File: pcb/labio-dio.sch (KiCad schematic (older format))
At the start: 103 parts, among them P601 CONN_01X02, P602 CONN_01X02, P603 CONN_01X04, P604 CONN_01X02, P605 CONN_01X03, P606 CONN_01X03, P607 CONN_01X05, P608 CONN_01X05, Q601 Q_NMOS_GSD, Q602 Q_NMOS_GSD, Q603 Q_NMOS_GSD, Q604 Q_NMOS_GSD, Q605 Q_NMOS_GSD, Q606 Q_NMOS_GSD, Q607 Q_NMOS_GSD, Q608 Q_NMOS_GSD, Q609 Q_NMOS_GSD, Q610 Q_NMOS_GSD, Q611 Q_NMOS_GSD, Q612 Q_NMOS_GSD, Q613 Q_NMOS_GSD, SW601 DIP_SWITCH_X04, SW602 DIP_SWITCH_X04, SW603 DIP_SWITCH_X04, SW604 DIP_SWITCH_X04, SW605 ROT_ENC, SW606 DIP_SWITCH_X04, U601 L298P_PowerSO20

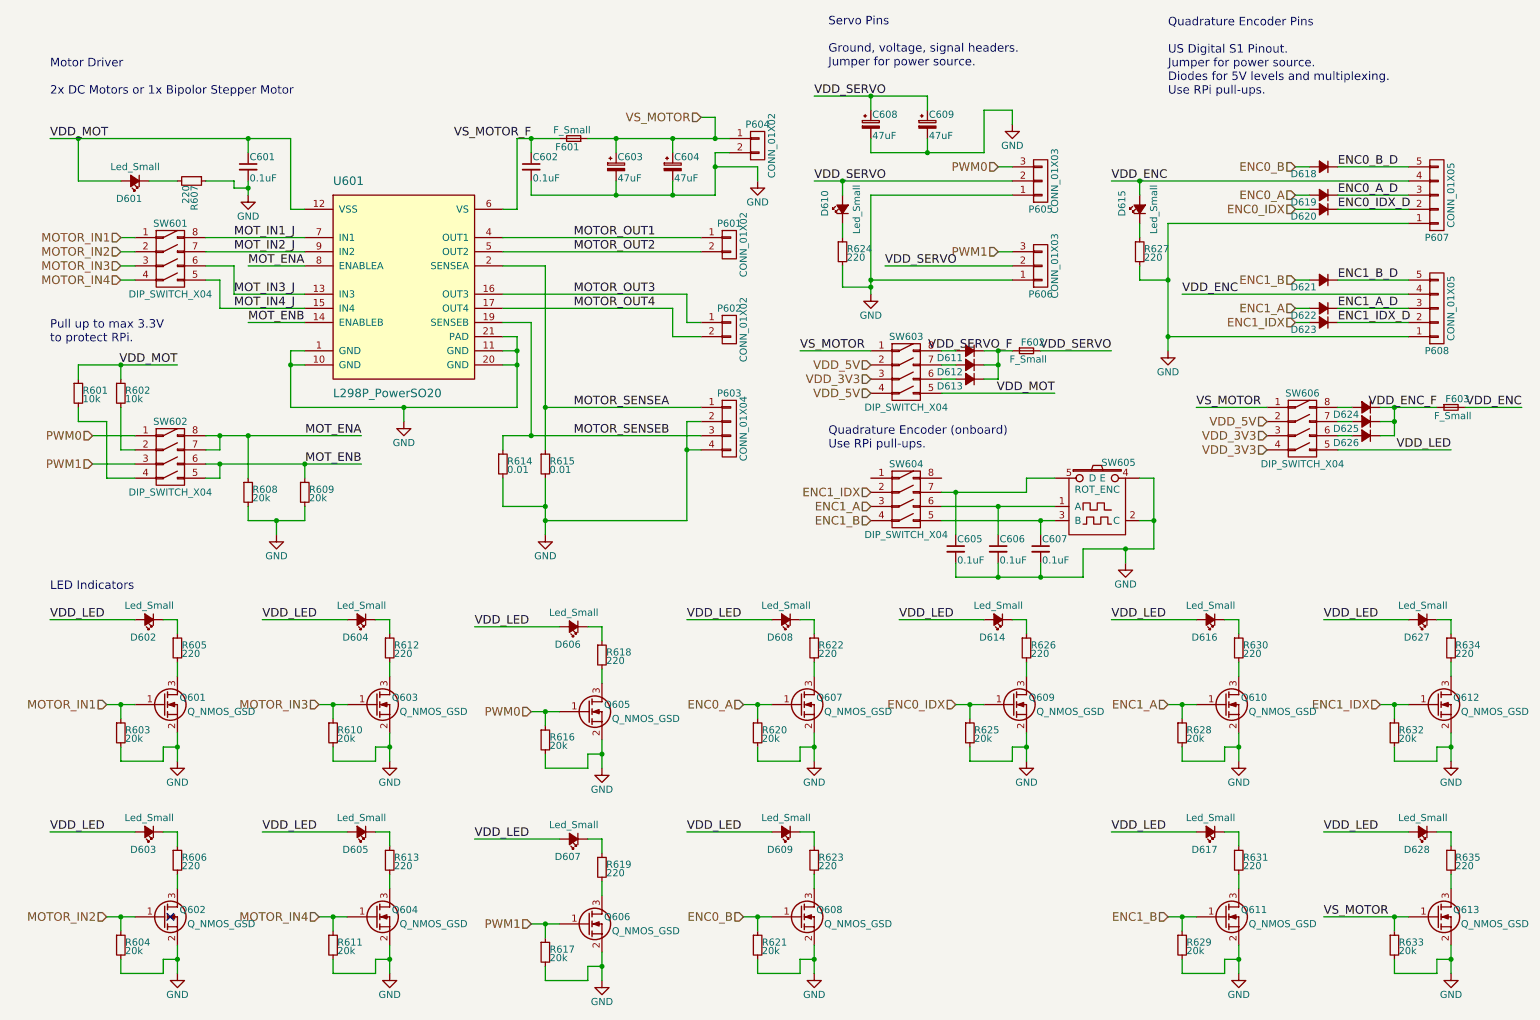
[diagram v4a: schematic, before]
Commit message: Fix ADC reading mic, possible backpowering, encoder pull downs, vias in footprint:
* Mic needs on-board path to ADC. Add proper bias and amp. Connect to ADC or codec with switches.
* Mic footprint (U701) flipped. Redraw footprint and adjust routing.
* Remove power from dip switches and replace with fuses. Turning power off to a block could result in backpower from driven IO lines.
* Remove/adjust pull downs on LEDs for encoder/dpad lines.
* Move vias out of display connector (P401) footprint.
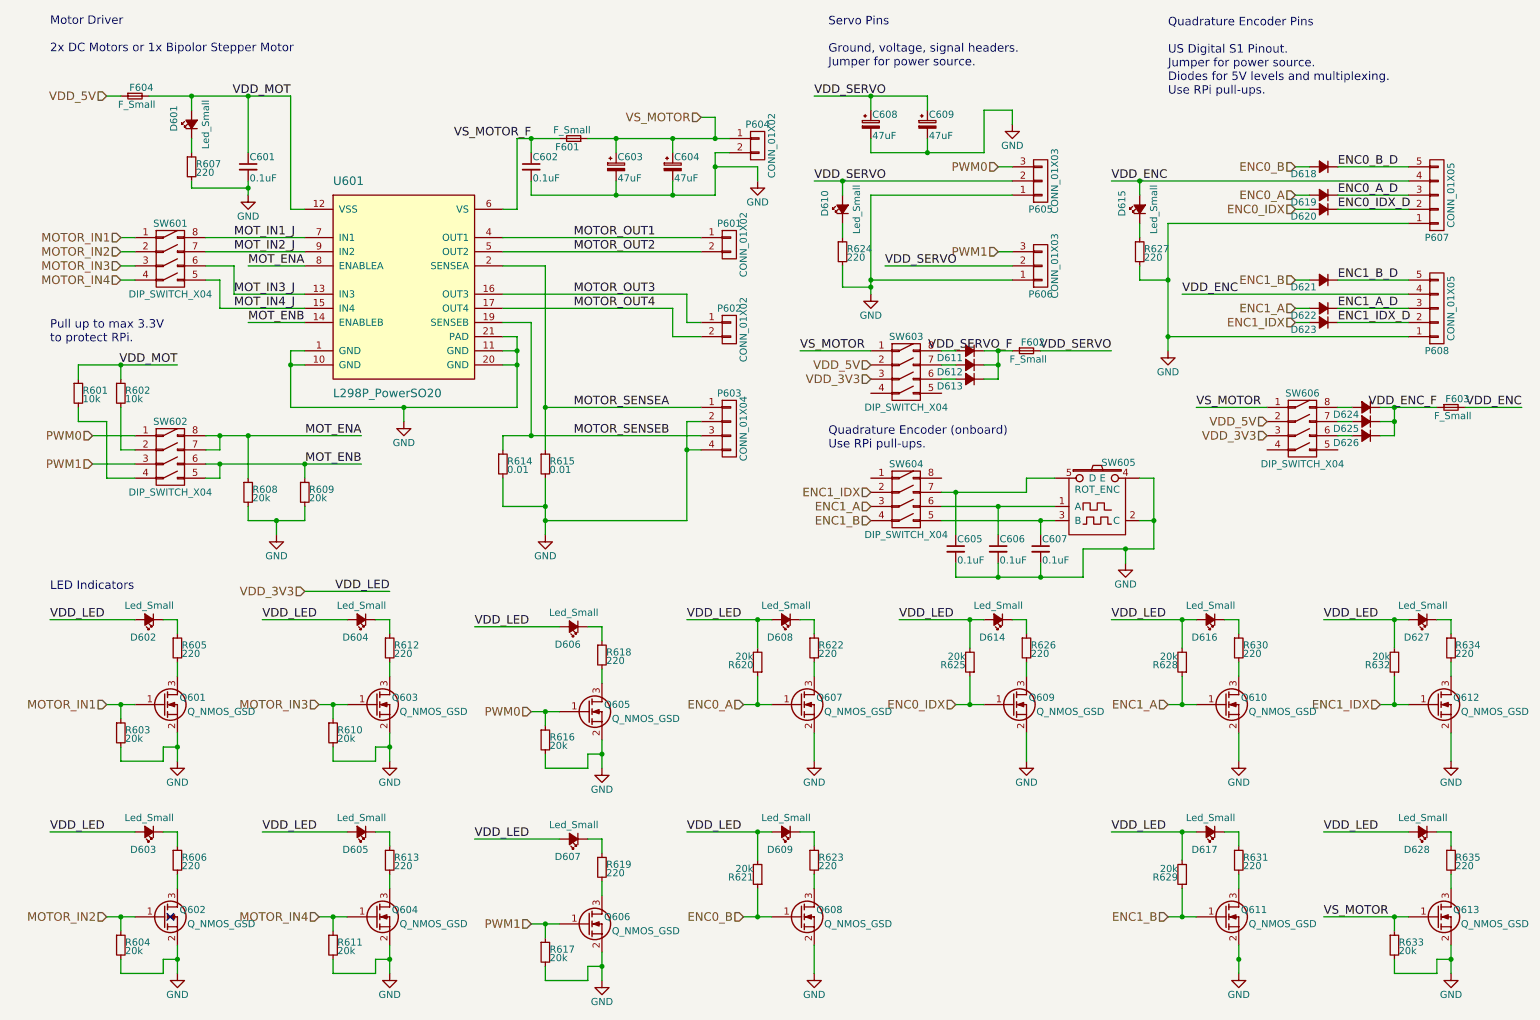
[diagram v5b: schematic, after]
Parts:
- added F604: F_Small, Resistors_SMD:R_1206, symbol F_Small
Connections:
- net GND: now also R607.2; no longer R607.1, R620.2, R621.2, R625.2, R628.2, R629.2, R632.2
- net VDD_3V3: now also D602.2 (A), D603.2 (A), D604.2 (A), D605.2 (A), D606.2 (A), D607.2 (A), D608.2 (A), D609.2 (A), D614.2 (A), D616.2 (A), D617.2 (A), D627.2 (A), D628.2 (A), R620.2, R621.2, R625.2, R628.2, R629.2, R632.2; no longer SW606.4 (4A)
- net VDD_5V: now also F604.1; no longer SW603.4 (4A)
- net VDD_MOT: now also F604.2; no longer SW603.5 (4B)
- net at D601.1 (K): now also R607.1; no longer R607.2
- removed net VDD_LED: D602.2 (A), D603.2 (A), D604.2 (A), D605.2 (A), D606.2 (A), D607.2 (A), D608.2 (A), D609.2 (A), D614.2 (A), D616.2 (A), D617.2 (A), D627.2 (A), D628.2 (A), SW606.5 (4B)
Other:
- moved on the sheet: D601, R607, R620, R621, R625, R628, R629, R632
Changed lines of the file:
@@
 encoding utf-8
 Sheet 6 10
-Title ""
+Title "Raspberry Pi Embedded Lab I/O"
 Date ""
-Rev ""
-Comp ""
+Rev "1.1.4"
+Comp "Carnegie Mellon University"
 Comment1 ""
-Comment2 ""
+Comment2 "Drawn by: Ian Hartwig"
 Comment3 ""
 Comment4 ""
@@
 Text Notes 6200 1000 0    60   ~ 0
 Servo Pins\n\nGround, voltage, signal headers.\nJumper for power source.
-Text Notes 700  1200 0    60   ~ 0
+Text Notes 700  900  0    60   ~ 0
 Motor Driver\n\n2x DC Motors or 1x Bipolor Stepper Motor
 $Comp
@@
 	1    0    0    -1
 $EndComp
-Text Label 7800 3300 2    60   ~ 0
-VDD_MOT
 Text Label 1600 3100 2    60   ~ 0
 VDD_MOT
-Text Label 700  1500 0    60   ~ 0
+Text Label 2400 1200 2    60   ~ 0
 VDD_MOT
-Text HLabel 9300 3700 0    60   Input ~ 0
+Text HLabel 2500 4700 0    60   Input ~ 0
 VDD_3V3
-Text Label 10600 3700 2    60   ~ 0
+Text Label 3100 4700 2    60   ~ 0
 VDD_LED
 Text Label 700  6400 0    60   ~ 0
@@
 L R_Small R620
 U 1 1 576F8F6D
-P 5700 5700
-F 0 "R620" H 5730 5720 50  0000 L CNN
-F 1 "20k" H 5730 5660 50  0000 L CNN
-F 2 "Resistors_SMD:R_0603" H 5700 5700 50  0001 C CNN
-F 3 "" H 5700 5700 50  0000 C CNN
-	1    5700 5700
-	1    0    0    -1
+P 5700 5200
+F 0 "R620" H 5730 5220 50  0000 L CNN
+F 1 "20k" H 5730 5160 50  0000 L CNN
+F 2 "Resistors_SMD:R_0603" H 5700 5200 50  0001 C CNN
+F 3 "" H 5700 5200 50  0000 C CNN
+	1    5700 5200
+	-1   0    0    1
 $EndComp
 $Comp
@@
 L R_Small R621
 U 1 1 576F8F95
-P 5700 7200
-F 0 "R621" H 5730 7220 50  0000 L CNN
-F 1 "20k" H 5730 7160 50  0000 L CNN
-F 2 "Resistors_SMD:R_0603" H 5700 7200 50  0001 C CNN
-F 3 "" H 5700 7200 50  0000 C CNN
-	1    5700 7200
-	1    0    0    -1
+P 5700 6700
+F 0 "R621" H 5730 6720 50  0000 L CNN
+F 1 "20k" H 5730 6660 50  0000 L CNN
+F 2 "Resistors_SMD:R_0603" H 5700 6700 50  0001 C CNN
+F 3 "" H 5700 6700 50  0000 C CNN
+	1    5700 6700
+	-1   0    0    1
 $EndComp
 Text Label 5200 6400 0    60   ~ 0
@@
 L R_Small R625
 U 1 1 576FAF6D
-P 7200 5700
-F 0 "R625" H 7230 5720 50  0000 L CNN
-F 1 "20k" H 7230 5660 50  0000 L CNN
-F 2 "Resistors_SMD:R_0603" H 7200 5700 50  0001 C CNN
-F 3 "" H 7200 5700 50  0000 C CNN
-	1    7200 5700
-	1    0    0    -1
+P 7200 5200
+F 0 "R625" H 7230 5220 50  0000 L CNN
+F 1 "20k" H 7230 5160 50  0000 L CNN
+F 2 "Resistors_SMD:R_0603" H 7200 5200 50  0001 C CNN
+F 3 "" H 7200 5200 50  0000 C CNN
+	1    7200 5200
+	-1   0    0    1
 $EndComp
 Text Label 6700 4900 0    60   ~ 0
@@
 L R_Small R628
 U 1 1 576FAF9A
-P 8700 5700
-F 0 "R628" H 8730 5720 50  0000 L CNN
-F 1 "20k" H 8730 5660 50  0000 L CNN
-F 2 "Resistors_SMD:R_0603" H 8700 5700 50  0001 C CNN
-F 3 "" H 8700 5700 50  0000 C CNN
-	1    8700 5700
-	1    0    0    -1
+P 8700 5200
+F 0 "R628" H 8730 5220 50  0000 L CNN
+F 1 "20k" H 8730 5160 50  0000 L CNN
+F 2 "Resistors_SMD:R_0603" H 8700 5200 50  0001 C CNN
+F 3 "" H 8700 5200 50  0000 C CNN
+	1    8700 5200
+	-1   0    0    1
 $EndComp
 Text Label 8200 4900 0    60   ~ 0
@@
 L R_Small R632
 U 1 1 576FAFC7
-P 10200 5700
-F 0 "R632" H 10230 5720 50  0000 L CNN
-F 1 "20k" H 10230 5660 50  0000 L CNN
-F 2 "Resistors_SMD:R_0603" H 10200 5700 50  0001 C CNN
-F 3 "" H 10200 5700 50  0000 C CNN
-	1    10200 5700
-	1    0    0    -1
+P 10200 5200
+F 0 "R632" H 10230 5220 50  0000 L CNN
+F 1 "20k" H 10230 5160 50  0000 L CNN
+F 2 "Resistors_SMD:R_0603" H 10200 5200 50  0001 C CNN
+F 3 "" H 10200 5200 50  0000 C CNN
+	1    10200 5200
+	-1   0    0    1
 $EndComp
 Text Label 9700 4900 0    60   ~ 0
@@
 L R_Small R629
 U 1 1 576FAFF4
-P 8700 7200
-F 0 "R629" H 8730 7220 50  0000 L CNN
-F 1 "20k" H 8730 7160 50  0000 L CNN
-F 2 "Resistors_SMD:R_0603" H 8700 7200 50  0001 C CNN
-F 3 "" H 8700 7200 50  0000 C CNN
-	1    8700 7200
-	1    0    0    -1
+P 8700 6700
+F 0 "R629" H 8730 6720 50  0000 L CNN
+F 1 "20k" H 8730 6660 50  0000 L CNN
+F 2 "Resistors_SMD:R_0603" H 8700 6700 50  0001 C CNN
+F 3 "" H 8700 6700 50  0000 C CNN
+	1    8700 6700
+	-1   0    0    1
 $EndComp
 Text Label 8200 6400 0    60   ~ 0
@@
 L Led_Small D601
 U 1 1 57708D41
-P 1300 1800
-F 0 "D601" H 1250 1925 50  0000 L CNN
-F 1 "Led_Small" H 1125 1700 50  0000 L CNN
-F 2 "LEDs:LED-0603" V 1300 1800 50  0001 C CNN
-F 3 "" V 1300 1800 50  0000 C CNN
-	1    1300 1800
-	-1   0    0    1
+P 1700 1400
+F 0 "D601" H 1650 1525 50  0000 L CNN
+F 1 "Led_Small" H 1525 1300 50  0000 L CNN
+F 2 "LEDs:LED-0603" V 1700 1400 50  0001 C CNN
+F 3 "" V 1700 1400 50  0000 C CNN
+	1    1700 1400
+	0    -1   -1   0
 $EndComp
 $Comp
 L R_Small R607
 U 1 1 57708E84
-P 1700 1800
-F 0 "R607" H 1730 1820 50  0000 L CNN
-F 1 "220" H 1730 1760 50  0000 L CNN
-F 2 "Resistors_SMD:R_0603" H 1700 1800 50  0001 C CNN
-F 3 "" H 1700 1800 50  0000 C CNN
-	1    1700 1800
-	0    1    1    0
+P 1700 1700
+F 0 "R607" H 1730 1720 50  0000 L CNN
+F 1 "220" H 1730 1660 50  0000 L CNN
+F 2 "Resistors_SMD:R_0603" H 1700 1700 50  0001 C CNN
+F 3 "" H 1700 1700 50  0000 C CNN
+	1    1700 1700
+	1    0    0    -1
 $EndComp
 $Comp
@@
 Connection ~ 2100 1850
 Wire Wire Line
-	2000 1850 2100 1850
-Wire Wire Line
-	2000 1800 2000 1850
-Wire Wire Line
-	1800 1800 2000 1800
-Wire Wire Line
-	1400 1800 1600 1800
-Connection ~ 900  1500
-Wire Wire Line
-	900  1800 900  1500
-Wire Wire Line
-	1200 1800 900  1800
+	1700 1850 2100 1850
 Wire Wire Line
 	10300 6400 9700 6400
@@
 Connection ~ 8700 7000
 Wire Wire Line
-	8700 7000 8700 7100
-Wire Wire Line
 	8600 7000 8800 7000
 Connection ~ 9100 7300
 Wire Wire Line
-	9000 7300 9100 7300
-Wire Wire Line
-	9000 7400 9000 7300
-Wire Wire Line
-	8700 7400 9000 7400
-Wire Wire Line
-	8700 7300 8700 7400
-Wire Wire Line
 	9100 6400 9000 6400
 Wire Wire Line
@@
 Connection ~ 10200 5500
 Wire Wire Line
-	10200 5500 10200 5600
-Wire Wire Line
 	10100 5500 10300 5500
-Connection ~ 10600 5800
-Wire Wire Line
-	10500 5800 10600 5800
-Wire Wire Line
-	10500 5900 10500 5800
-Wire Wire Line
-	10200 5900 10500 5900
-Wire Wire Line
-	10200 5800 10200 5900
 Wire Wire Line
 	10600 4900 10500 4900
@@
 Connection ~ 8700 5500
 Wire Wire Line
-	8700 5500 8700 5600
-Wire Wire Line
 	8600 5500 8800 5500
-Connection ~ 9100 5800
-Wire Wire Line
-	9000 5800 9100 5800
-Wire Wire Line
-	9000 5900 9000 5800
-Wire Wire Line
-	8700 5900 9000 5900
-Wire Wire Line
-	8700 5800 8700 5900
 Wire Wire Line
 	9100 4900 9000 4900
@@
 Connection ~ 7200 5500
 Wire Wire Line
-	7200 5500 7200 5600
-Wire Wire Line
 	7100 5500 7300 5500
-Connection ~ 7600 5800
-Wire Wire Line
-	7500 5800 7600 5800
-Wire Wire Line
-	7500 5900 7500 5800
-Wire Wire Line
-	7200 5900 7500 5900
-Wire Wire Line
-	7200 5800 7200 5900
 Wire Wire Line
 	7600 4900 7500 4900
@@
 Connection ~ 5700 7000
 Wire Wire Line
-	5700 7000 5700 7100
-Wire Wire Line
 	5600 7000 5800 7000
 Connection ~ 4200 7050
@@
 Connection ~ 5700 5500
 Wire Wire Line
-	5700 5500 5700 5600
-Wire Wire Line
 	5600 5500 5800 5500
-Connection ~ 6100 7300
-Wire Wire Line
-	6000 7300 6100 7300
-Wire Wire Line
-	6000 7400 6000 7300
-Wire Wire Line
-	5700 7400 6000 7400
-Wire Wire Line
-	5700 7300 5700 7400
 Wire Wire Line
 	6100 6400 6000 6400
@@
 Wire Wire Line
 	6100 7200 6100 7400
-Connection ~ 6100 5800
-Wire Wire Line
-	6000 5800 6100 5800
-Wire Wire Line
-	6000 5900 6000 5800
-Wire Wire Line
-	5700 5900 6000 5900
-Wire Wire Line
-	5700 5800 5700 5900
 Wire Wire Line
 	6100 4900 6000 4900
@@
 Wire Wire Line
 	1300 4900 700  4900
-Wire Wire Line
-	9800 3700 10600 3700
-Wire Wire Line
-	7000 3300 7800 3300
 Connection ~ 1200 5500
 Wire Wire Line
@@
 Wire Wire Line
 	9500 2800 9600 2800
-Connection ~ 2100 1500
-Wire Wire Line
-	2100 1500 2100 1600
-Wire Wire Line
-	700  1500 2400 1500
-Wire Wire Line
-	2400 1500 2400 2000
+Wire Wire Line
+	2100 1200 2100 1600
+Wire Wire Line
+	2400 1200 2400 2000
 Wire Wire Line
 	2400 2000 2500 2000
@@
 Text Notes 700  2950 0    60   ~ 0
 Pull up to max 3.3V\nto protect RPi.
-Text HLabel 6500 3300 0    60   Input ~ 0
+Text HLabel 1100 1200 0    60   Input ~ 0
 VDD_5V
 $Comp
@@
 Wire Wire Line
 	4100 1800 4100 1900
+Wire Wire Line
+	2500 4700 3100 4700
+$Comp
+L F_Small F604
+U 1 1 57AFC1F2
+P 1300 1200
+F 0 "F604" H 1260 1260 50  0000 L CNN
+F 1 "F_Small" H 1180 1140 50  0000 L CNN
+F 2 "Resistors_SMD:R_1206" H 1300 1200 50  0001 C CNN
+F 3 "" H 1300 1200 50  0000 C CNN
+	1    1300 1200
+	1    0    0    -1
+$EndComp
+Wire Wire Line
+	1700 1800 1700 1850
+Wire Wire Line
+	1700 1500 1700 1600
+Wire Wire Line
+	1100 1200 1200 1200
+Wire Wire Line
+	1400 1200 2400 1200
+Wire Wire Line
+	1700 1200 1700 1300
+Connection ~ 1700 1200
+Connection ~ 2100 1200
+Wire Wire Line
+	5700 6600 5700 6400
+Connection ~ 5700 6400
+Wire Wire Line
+	5700 6800 5700 7000
+Wire Wire Line
+	5700 5100 5700 4900
+Connection ~ 5700 4900
+Wire Wire Line
+	5700 5300 5700 5500
+Wire Wire Line
+	7200 5100 7200 4900
+Connection ~ 7200 4900
+Wire Wire Line
+	7200 5300 7200 5500
+Wire Wire Line
+	8700 5100 8700 4900
+Connection ~ 8700 4900
+Wire Wire Line
+	8700 5500 8700 5300
+Wire Wire Line
+	10200 5300 10200 5500
+Wire Wire Line
+	10200 5100 10200 4900
+Connection ~ 10200 4900
+Wire Wire Line
+	8700 6600 8700 6400
+Connection ~ 8700 6400
+Wire Wire Line
+	8700 7000 8700 6800
 $EndSCHEMATC
